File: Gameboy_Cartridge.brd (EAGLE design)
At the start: 49.3 x 48 mm, 10 parts, among them IC1 AT49F040J

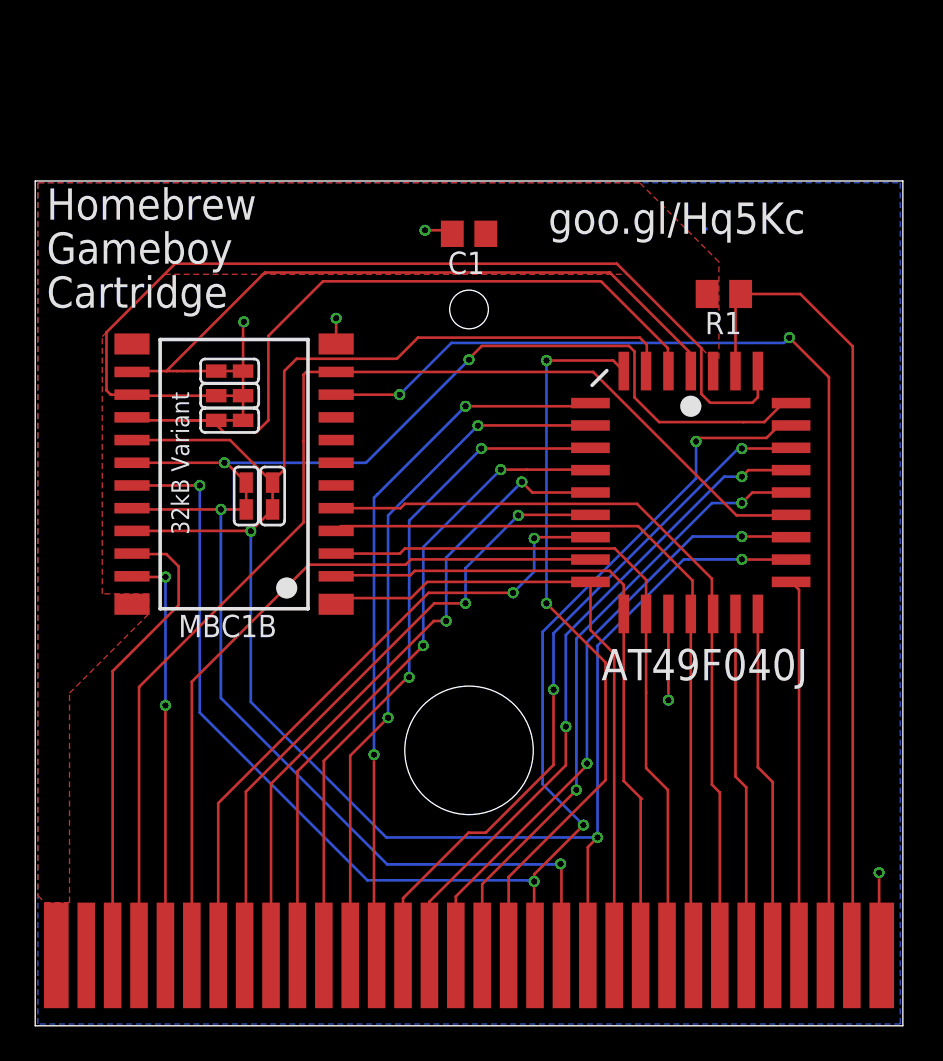
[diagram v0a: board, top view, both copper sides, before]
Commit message: Moved solder jumper outside of the DMG01 chip.
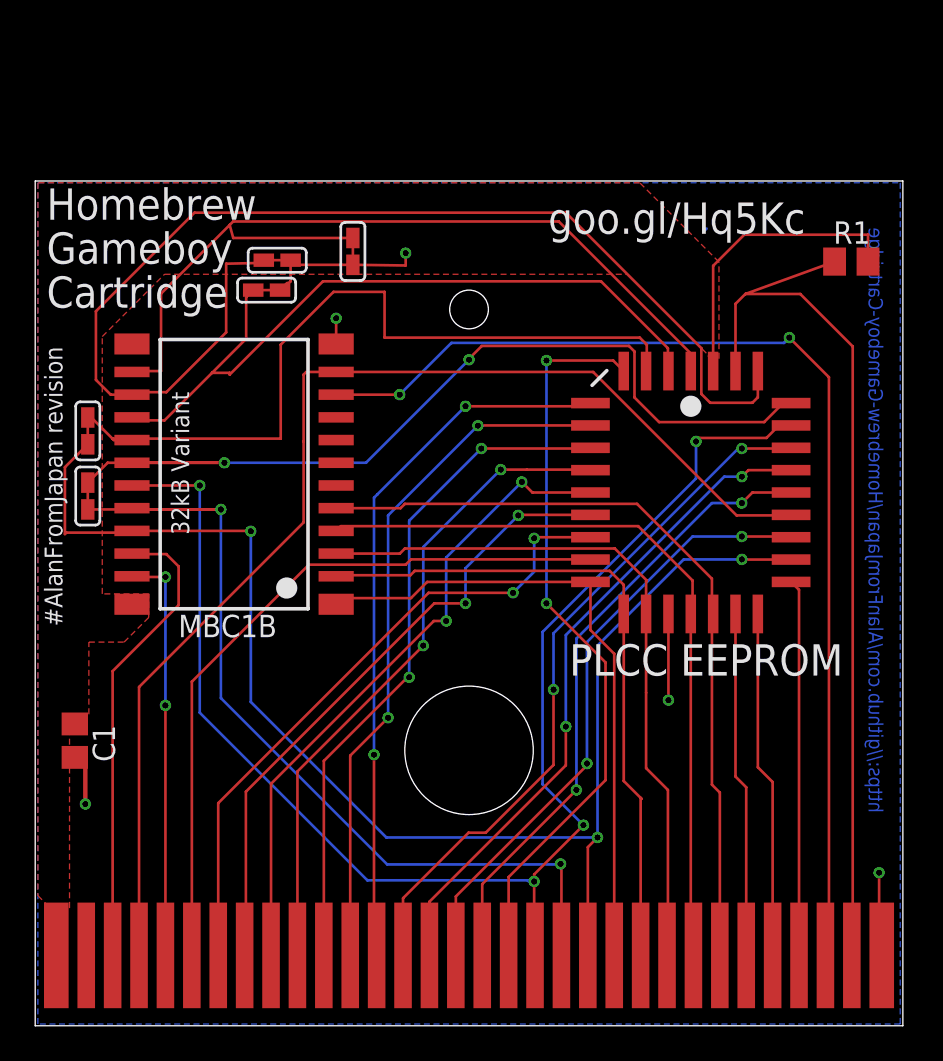
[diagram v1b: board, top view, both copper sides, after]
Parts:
- moved C1 36.5 mm to (3.10, 16.2), turned to 270 degrees
- moved SJ4 11.1 mm to (3.84, 33.8)
- moved SJ1 9.76 mm to (18.9, 44.0), turned to 270 degrees
- moved SJ5 9.00 mm to (3.84, 30.1)
- moved SJ2 8.16 mm to (14.6, 43.5)
- moved SJ3 7.69 mm to (14.0, 41.8)
- moved R1 7.47 mm to (47.2, 43.4), turned to 0 degrees
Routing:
- net VDD: track 0.00 -> 17.0 mm
- net B: track 54.7 -> 66.8 mm
- net A: track 39.8 -> 49.5 mm
- net 21: track 72.0 -> 79.8 mm
- net E: track 45.7 -> 52.2 mm
- net 20: track 45.7 -> 51.8 mm
- net D: track 39.7 -> 44.8 mm
- net 31: track 46.8 -> 52.0 mm
- net GND: track 18.8 -> 23.7 mm
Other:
- board text added: "#AlanFromJapan revision"
- board text added: "PLCC EEPROM"
- board text added: "https://github.com/AlanFromJapan/Homebrew-Gameboy-Cartridge"

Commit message: Changed a few details, hope I didn't screw it up...
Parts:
- added JP1: JUMPER-SMT_3_1-NC_TRACE_SILK, SparkFun-Jumpers:SMT-JUMPER_3_1-NC_TRACE_SILK
- added TP1: TEST-POINT3X5, SparkFun-Connectors:PAD.03X.05
- SJ1, SJ2, SJ3, SJ4, SJ5: value SOLDER-JUMPER -> JUMPER-SMT_2_NO_SILK; device gameboy:SJ -> SparkFun-Jumpers:SMT-JUMPER_2_NO_SILK
- moved C1 45.5 mm to (40.5, 42.2), turned to 0 degrees
- moved R1 1.67 mm to (46.5, 44.9), turned to 90 degrees
- moved SJ3 0.72 mm to (13.4, 41.4)
- moved SJ4 0.40 mm to (3.84, 33.4)
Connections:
- new net N$1: IC1.31, TP1.P$1
- new net N$2: IC1.22, JP1.2
- net 21: now also JP1.3; no longer IC1.22
- net 31: no longer IC1.31
- net GND: now also JP1.1
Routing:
- net 31: track 52.0 -> 40.8 mm
- net N$1: track 0.00 -> 8.90 mm
- net N$3: track 0.00 -> 7.70 mm, vias 0 -> 1
- net A: track 49.5 -> 43.3 mm
- net 21: track 79.8 -> 73.6 mm, vias 3 -> 2
- net VDD: track 17.0 -> 14.1 mm
- net GND: track 23.7 -> 26.3 mm
- net D: track 44.8 -> 43.4 mm
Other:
- board text added: "#v1.0 April2020"
- board text added: "/CS"
- board text added: "/RD"
- board text added: "/WE"
- board text added: "/WR"
- board text added: "A0"
- board text added: "A15"
- board text added: "Audio_In"
- board text added: "Clock"
- board text added: "D0"
- board text added: "D7"
- board text added: "Gnd"
- board text added: "Reset"
- board text added: "Vcc"
